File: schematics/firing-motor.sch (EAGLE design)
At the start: 22 parts, among them IC1 4011D, IC2 OPA642N, IC3 OPA642N

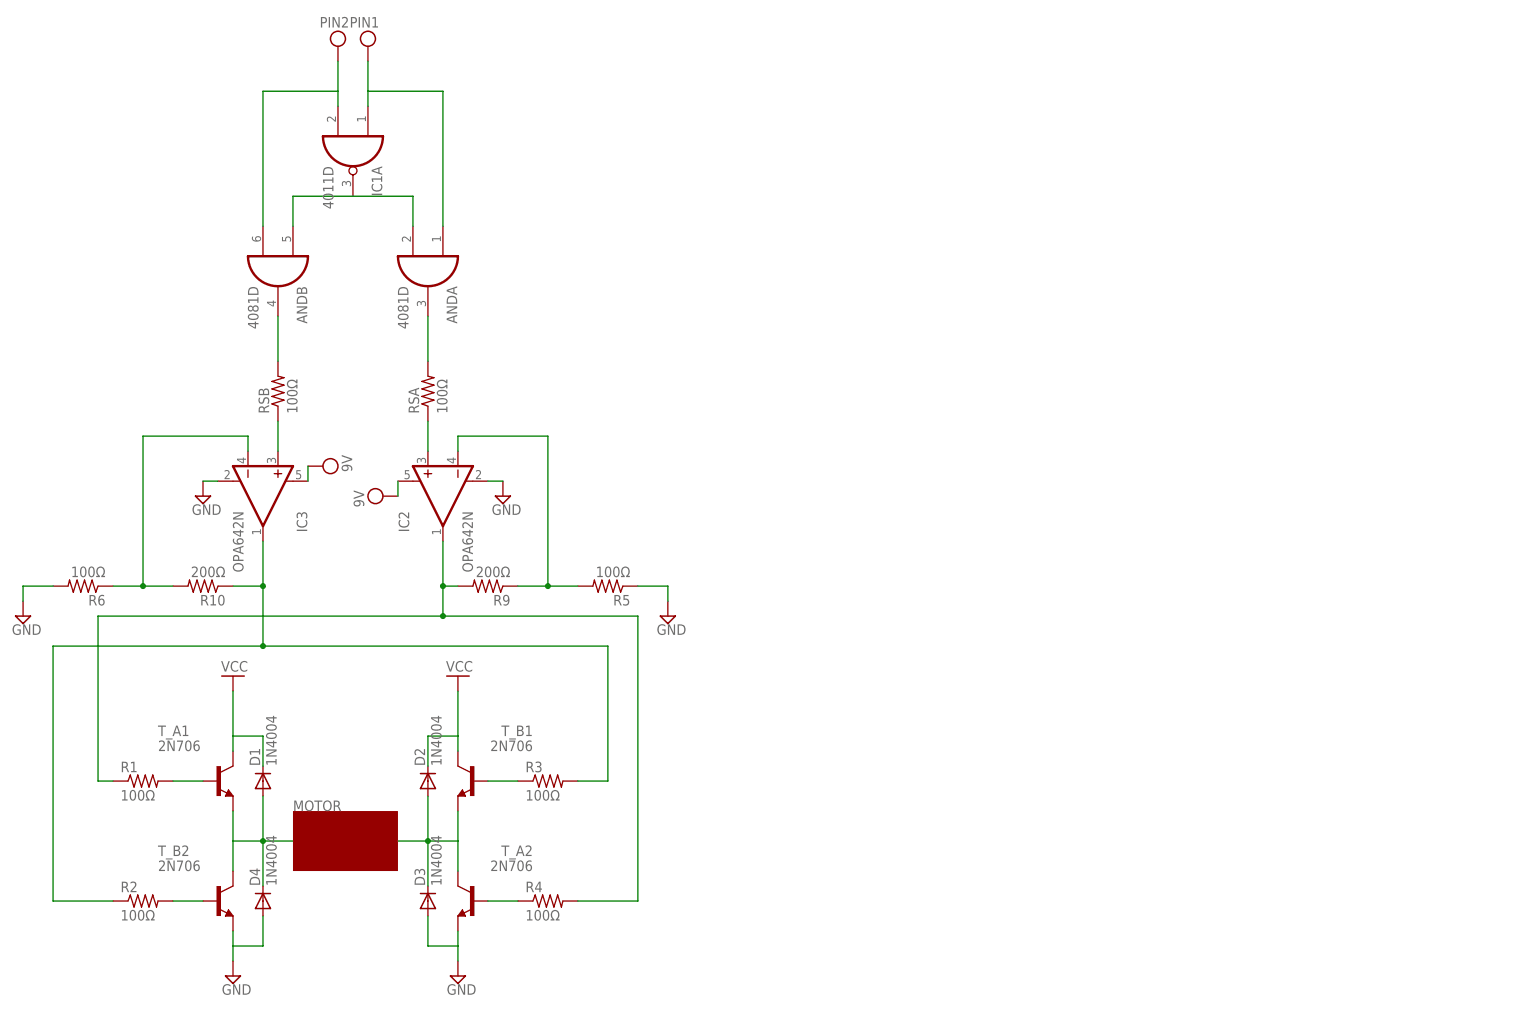
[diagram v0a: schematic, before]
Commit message: Worked on final proposal, started high-level diagram of circuitry.  Need button circuitry; will finish at next meeting.
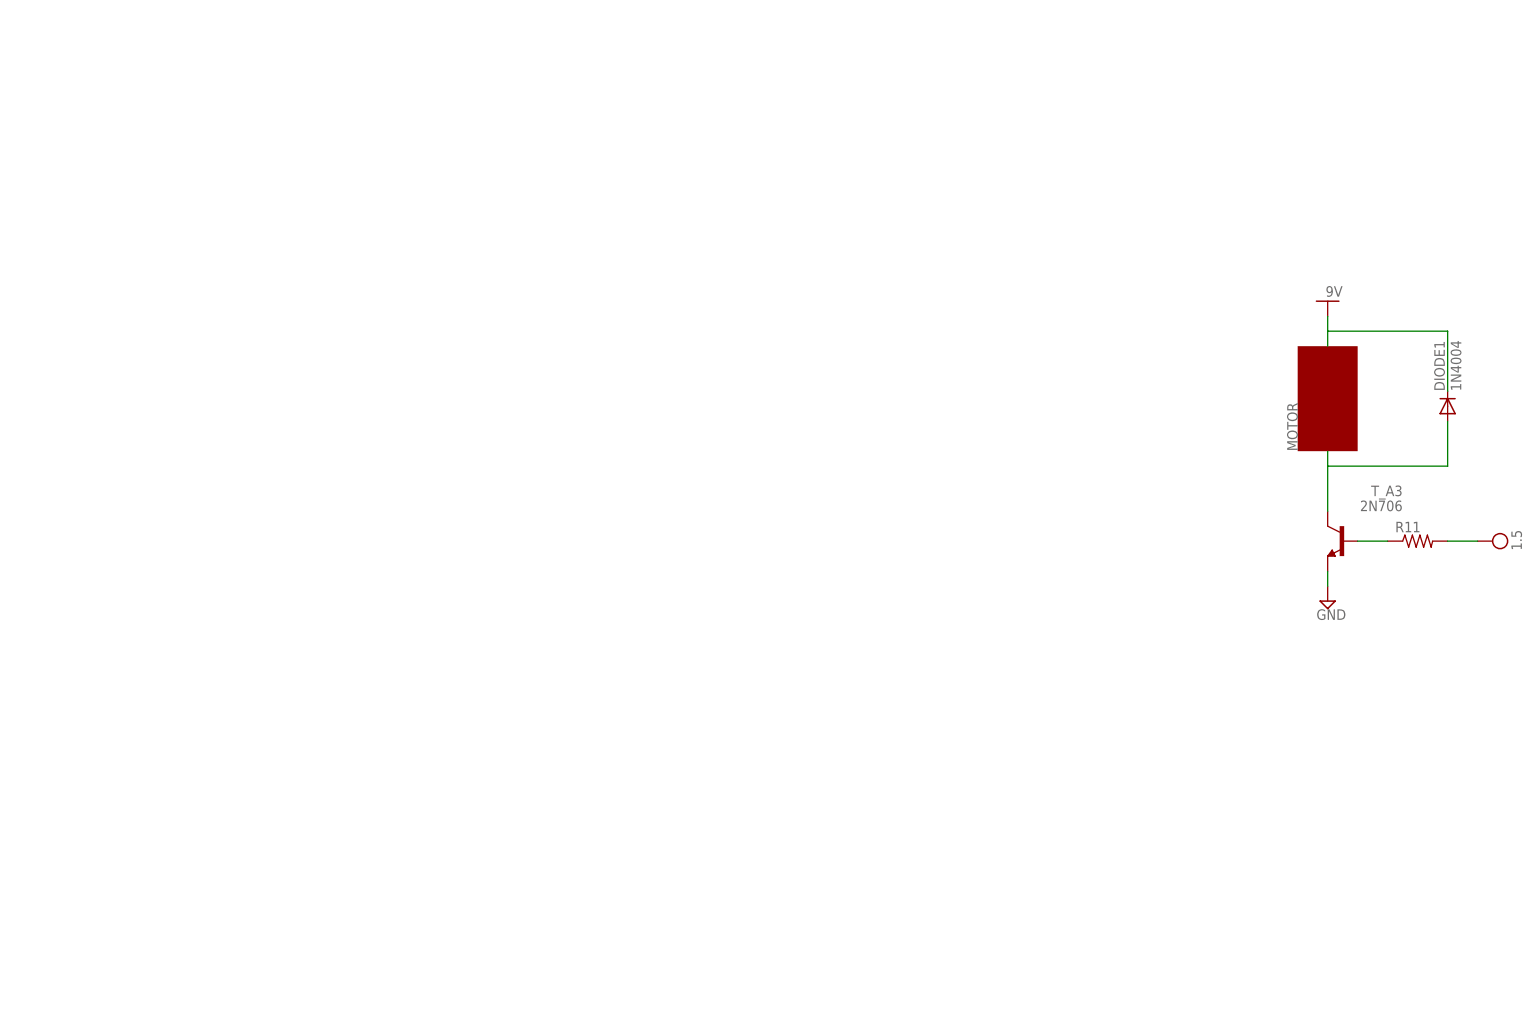
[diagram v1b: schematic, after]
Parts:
- removed AND: 4081D, 40xx:4081D
- removed D1, D2, D3, D4: 1N4004, diode:1N4004
- removed IC1: 4011D, 40xx:4011D
- removed IC2, IC3: OPA642N, burr-brown:OPA642N
- removed R1, R2, R3, R4, R5, R6, RSA, RSB: 100Ω, rcl:R-US_0204/2V
- removed R10, R9: 200Ω, rcl:R-US_0204/2V
- removed T_A1, T_A2, T_B1, T_B2: 2N706, transistor:2N706
- added DIODE1: 1N4004, diode:1N4004
- added R11: (no value), rcl:R-US_0204/2V
- added T_A3: 2N706, transistor:2N706
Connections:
- removed net N$1: D2.A, D3.C, T_A2.C, T_B1.E
- removed net N$10: ANDB.O, RSB.2
- removed net N$11: ANDA.O, RSA.2
- removed net N$12: IC2.+IN, RSA.1
- removed net N$13: IC3.+IN, RSB.1
- removed net N$14: IC3.-IN, R10.2, R6.1
- removed net N$15: IC2.-IN, R5.2, R9.1
- removed net N$2: D1.A, D4.C, T_A1.E, T_B2.C
- removed net N$3: R4.1, T_A2.B
- removed net N$4: R3.1, T_B1.B
- removed net N$5: R1.2, T_A1.B
- removed net N$6: R2.2, T_B2.B
- removed net N$7: ANDA.I1, ANDB.I0, IC1A.O
- removed net N$8: IC3.OUT, R10.1, R2.1, R3.2
- removed net N$9: IC2.OUT, R1.1, R4.2, R9.2
- removed net VDD: ANDA.I0, ANDB.I1, IC1A.I0, IC1A.I1
- new net N$23: DIODE1.A, T_A3.C
- new net N$24: R11.1, T_A3.B
- net GND: now also DIODE1.C, T_A3.E; no longer D3.A, D4.A, IC2.V-, IC3.V-, R5.1, R6.2, T_A2.E, T_B2.E
- net VCC: now also R11.2; no longer D1.C, D2.C, IC2.V+, IC3.V+, T_A1.C, T_B1.C
